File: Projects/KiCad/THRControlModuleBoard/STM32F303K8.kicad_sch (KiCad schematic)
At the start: 1 part, among them U3 NUCLEO-F303K8

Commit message: THRControlModuleBoardの更新
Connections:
- net DRDY: now reaches U3.3_9 (PB1)
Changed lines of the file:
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@@
+    (stroke (width 0) (type default))
+  )
+  (wire (pts (xy 116.84 101.6) (xy 119.38 101.6))
     (stroke (width 0) (type default))
   )
@@
     (effects (font (size 1.27 1.27)) (justify left))
   )
+  (hierarchical_label "DRDY" (shape input) (at 116.84 101.6 180) (fields_autoplaced)
+    (effects (font (size 1.27 1.27)) (justify right))
+  )
   (hierarchical_label "SPI__SDI-MOSI" (shape output) (at 116.84 106.68 180) (fields_autoplaced)

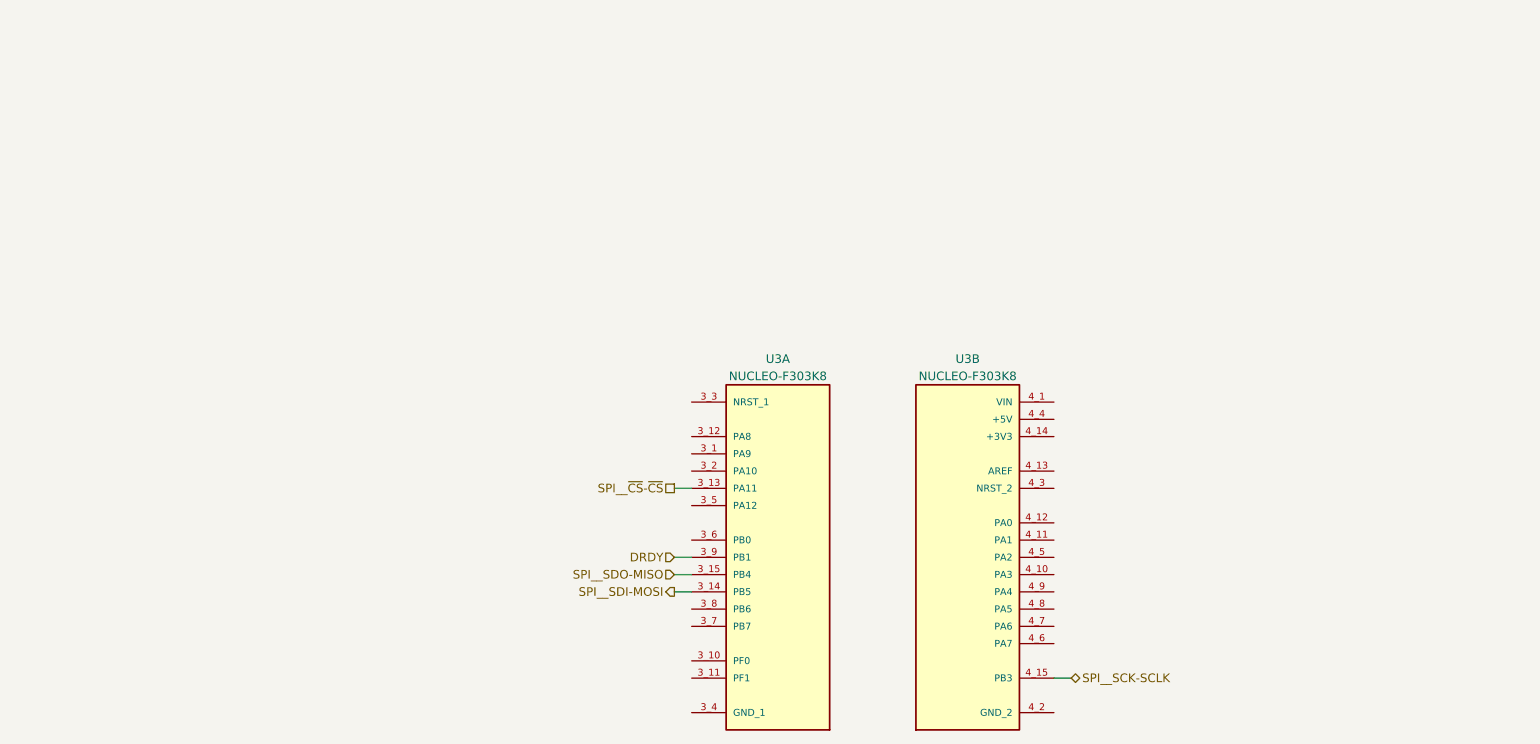
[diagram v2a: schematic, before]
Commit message: THRControlModuleBoardにRS485系統を追加しました。
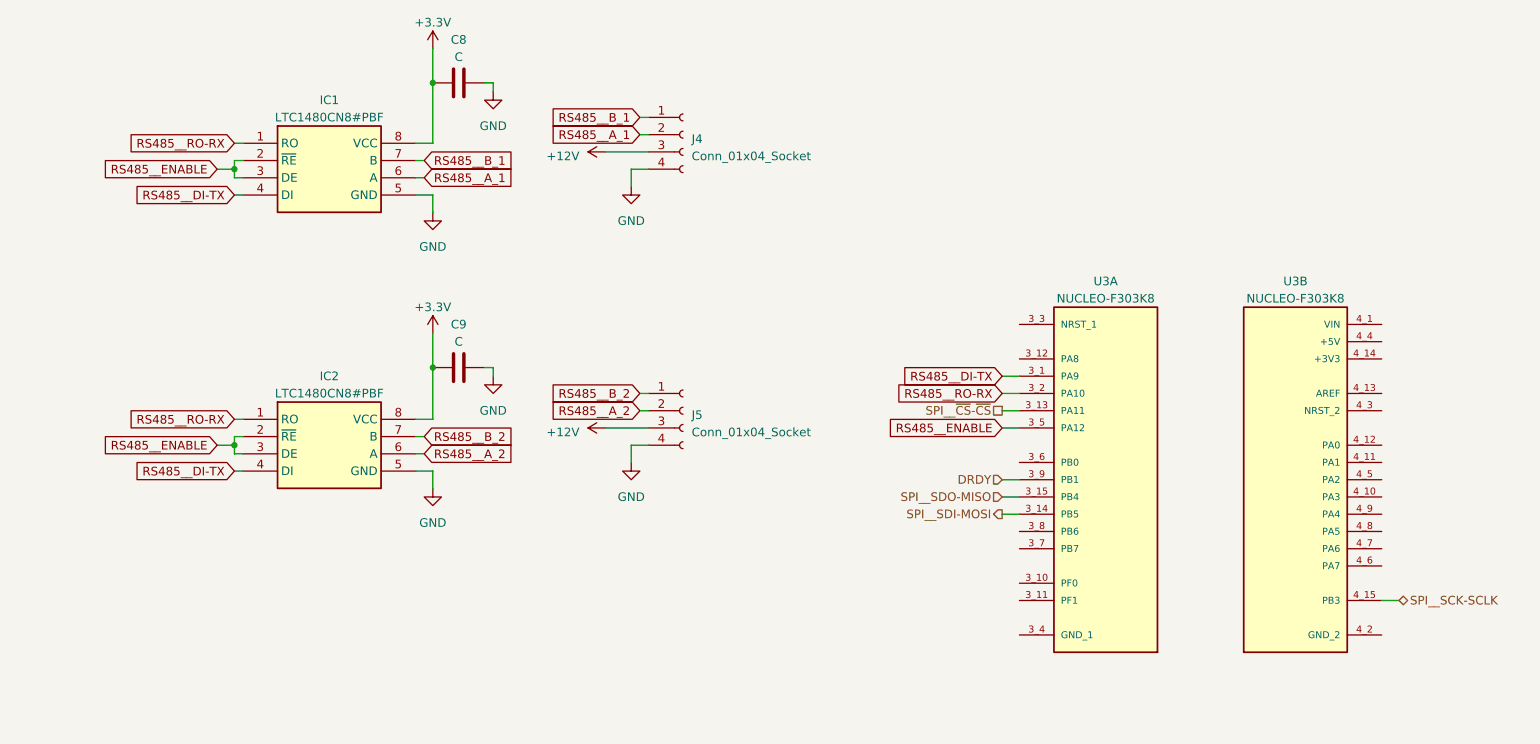
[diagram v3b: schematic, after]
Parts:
- added C8, C9: C, symbol Device:C
- added IC1, IC2: LTC1480CN8#PBF, DIP794W53P254L1016H394Q8N, symbol LTC1480CN8#PBF:LTC1480CN8#PBF
- added J4, J5: Conn_01x04_Socket, CONNECTOR:CONNECTOR_4-STRAIGHT, symbol Connector:Conn_01x04_Socket
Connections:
- net RS485__DI-TX: now reaches U3.3_1 (PA9)
- net RS485__DI-TX: now also IC1.4 (DI), IC2.4 (DI)
- net RS485__RO-RX: now reaches U3.3_2 (PA10)
- net RS485__RO-RX: now also IC1.1 (RO), IC2.1 (RO)
- net RS485__ENABLE: now reaches U3.3_5 (PA12)
- net RS485__ENABLE: now also IC1.2 (~{RE}), IC1.3 (DE), IC2.2 (~{RE}), IC2.3 (DE)
- new net +12V: J4.3 (Pin_3), J5.3 (Pin_3)
- new net +3.3V: C8.1, C9.1, IC1.8 (VCC), IC2.8 (VCC)
- new net GND: C8.2, C9.2, IC1.5 (GND), IC2.5 (GND), J4.4 (Pin_4), J5.4 (Pin_4)
- new net RS485__A_1: IC1.6 (A), J4.2 (Pin_2)
- new net RS485__A_2: IC2.6 (A), J5.2 (Pin_2)
- new net RS485__B_1: IC1.7 (B), J4.1 (Pin_1)
- new net RS485__B_2: IC2.7 (B), J5.1 (Pin_1)
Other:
- moved on the sheet: U3A, U3B

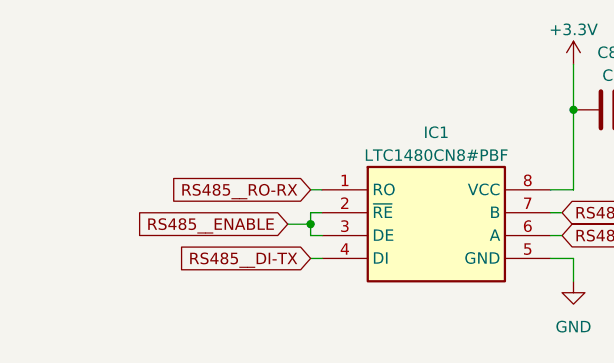
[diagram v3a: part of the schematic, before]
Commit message: THRControlModule-STM32F303K8の更新
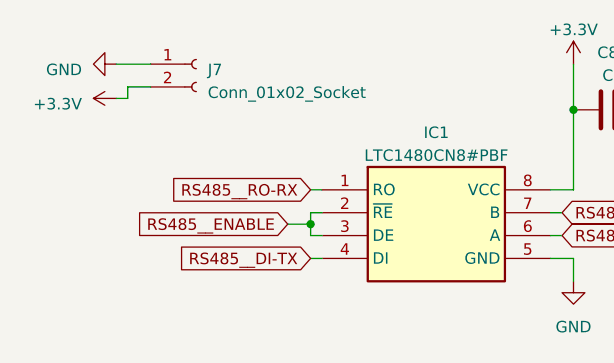
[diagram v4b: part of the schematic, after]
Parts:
- added J7: Conn_01x02_Socket, CONNECTOR:CONNECTOR_2-STRAIGHT, symbol Connector:Conn_01x02_Socket
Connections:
- net +3.3V: now also J7.2 (Pin_2)
- net GND: now also J7.1 (Pin_1)
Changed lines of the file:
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@@
+    (stroke (width 0) (type default))
+  )
+  (wire (pts (xy 30.48 26.67) (xy 34.29 26.67))
+    (stroke (width 0) (type default))
+  )
+  (wire (pts (xy 31.75 30.48) (xy 30.48 30.48))
     (stroke (width 0) (type default))
   )
@@
     (stroke (width 0) (type default))
   )
+  (wire (pts (xy 34.29 29.21) (xy 31.75 29.21))
+    (stroke (width 0) (type default))
+  )
   (wire (pts (xy 90.17 73.66) (xy 88.9 73.66))
     (stroke (width 0) (type default))
   )
   (wire (pts (xy 111.76 77.47) (xy 113.03 77.47))
+    (stroke (width 0) (type default))
+  )
+  (wire (pts (xy 31.75 29.21) (xy 31.75 30.48))
     (stroke (width 0) (type default))
   )
@@
     )
   )
+  (symbol (lib_id "power:+3.3V") (at 30.48 30.48 90) (unit 1)
+    (in_bom yes) (on_board yes) (dnp no) (fields_autoplaced)
+    (property "Reference" "#PWR032" (at 34.29 30.48 0)
+      (effects (font (size 1.27 1.27)) hide)
+    )
+    (property "Value" "+3.3V" (at 26.67 31.115 90)
+      (effects (font (size 1.27 1.27)) (justify left))
+    )
+    (property "Footprint" "" (at 30.48 30.48 0)
+      (effects (font (size 1.27 1.27)) hide)
+    )
+    (property "Datasheet" "" (at 30.48 30.48 0)
+      (effects (font (size 1.27 1.27)) hide)
+    )
+    (pin "1")
+    (instances
+      (project "THRControlModuleBoard"
+        (path "/79fd2516-dad6-414c-bb46-91ee9bfb5006"
+          (reference "#PWR032") (unit 1)
+        )
+        (path "/79fd2516-dad6-414c-bb46-91ee9bfb5006/f6014a5d-9cc0-416f-9341-c878d8d048fe"
+          (reference "#PWR034") (unit 1)
+        )
+      )
+    )
+  )
   (symbol (lib_id "Connector:Conn_01x04_Socket") (at 118.11 80.01 0) (unit 1)
     (in_bom yes) (on_board yes) (dnp no) (fields_autoplaced)
@@
         (path "/79fd2516-dad6-414c-bb46-91ee9bfb5006/f6014a5d-9cc0-416f-9341-c878d8d048fe"
           (reference "#PWR024") (unit 1)
+        )
+      )
+    )
+  )
+  (symbol (lib_id "Connector:Conn_01x02_Socket") (at 39.37 26.67 0) (unit 1)
+    (in_bom yes) (on_board yes) (dnp no) (fields_autoplaced)
+    (property "Reference" "J7" (at 40.64 27.305 0)
+      (effects (font (size 1.27 1.27)) (justify left))
+    )
+    (property "Value" "Conn_01x02_Socket" (at 40.64 29.845 0)
+      (effects (font (size 1.27 1.27)) (justify left))
+    )
+    (property "Footprint" "CONNECTOR:CONNECTOR_2-STRAIGHT" (at 39.37 26.67 0)
+      (effects (font (size 1.27 1.27)) hide)
+    )
+    (property "Datasheet" "~" (at 39.37 26.67 0)
+      (effects (font (size 1.27 1.27)) hide)
+    )
+    (pin "1")
+    (pin "2")
+    (instances
+      (project "THRControlModuleBoard"
+        (path "/79fd2516-dad6-414c-bb46-91ee9bfb5006"
+          (reference "J7") (unit 1)
+        )
+        (path "/79fd2516-dad6-414c-bb46-91ee9bfb5006/f6014a5d-9cc0-416f-9341-c878d8d048fe"
+          (reference "J8") (unit 1)
         )
       )
@@
         )
       )
+    )
+  )
+  (symbol (lib_id "power:GND") (at 30.48 26.67 270) (unit 1)
+    (in_bom yes) (on_board yes) (dnp no) (fields_autoplaced)
+    (property "Reference" "#PWR031" (at 24.13 26.67 0)
+      (effects (font (size 1.27 1.27)) hide)
+    )
+    (property "Value" "GND" (at 26.67 27.305 90)
+      (effects (font (size 1.27 1.27)) (justify right))
+    )
+    (property "Footprint" "" (at 30.48 26.67 0)
+      (effects (font (size 1.27 1.27)) hide)
+    )
+    (property "Datasheet" "" (at 30.48 26.67 0)
+      (effects (font (size 1.27 1.27)) hide)
+    )
+    (pin "1")
+    (instances
+      (project "THRControlModuleBoard"
+        (path "/79fd2516-dad6-414c-bb46-91ee9bfb5006"
+          (reference "#PWR031") (unit 1)
+        )
+        (path "/79fd2516-dad6-414c-bb46-91ee9bfb5006/f6014a5d-9cc0-416f-9341-c878d8d048fe"
+          (reference "#PWR033") (unit 1)
+        )
+      )
